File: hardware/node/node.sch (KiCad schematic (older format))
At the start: 48 parts, among them J1 IN, J10 ICSP, J30 PUMP, J60 OVF, Q0 SI2323DS, U1 ATmega328P-AU, U2 LMC555xM, U3 TPS22810, U4 P82B96

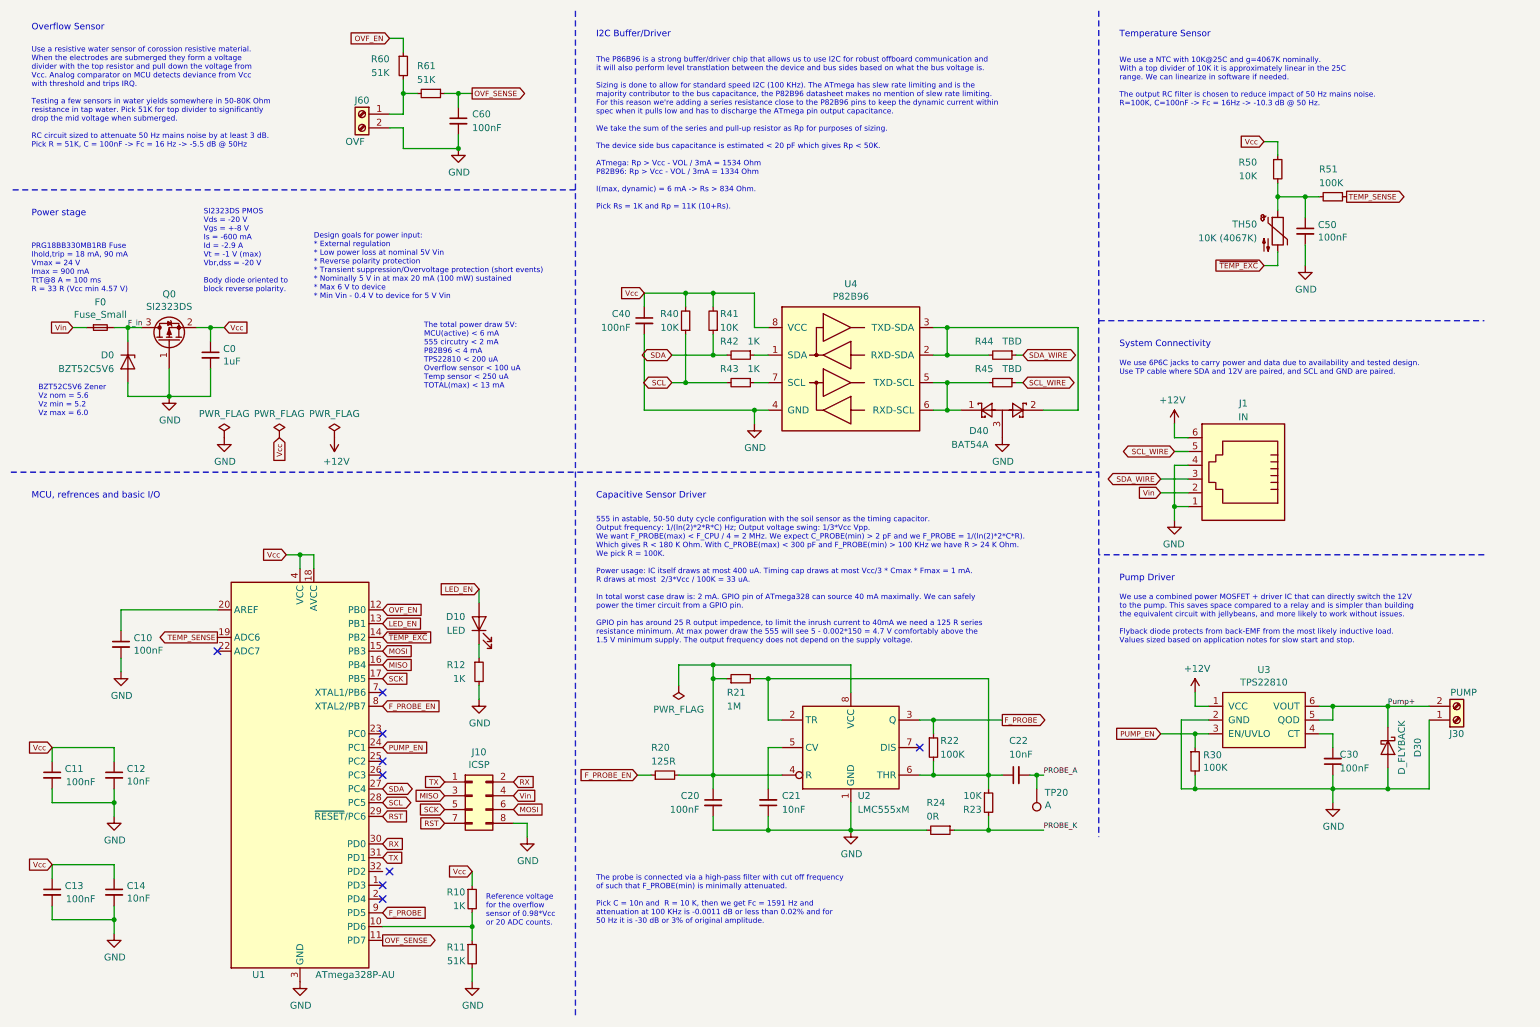
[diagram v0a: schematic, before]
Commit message: Updating layout of node and art.
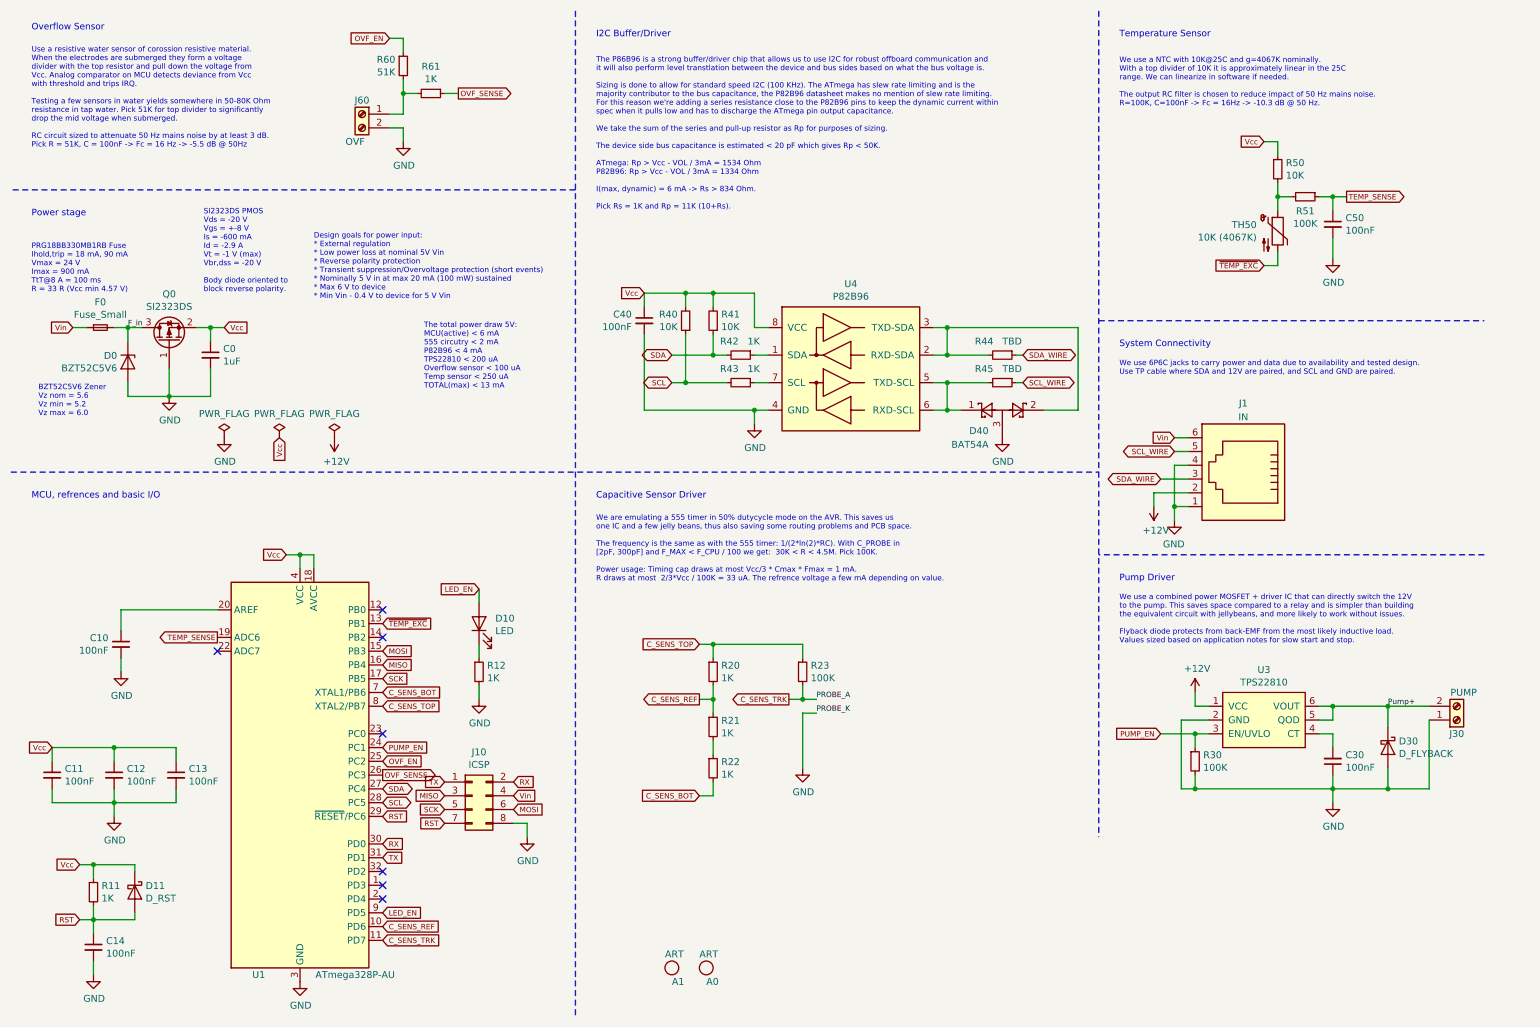
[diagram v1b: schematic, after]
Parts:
- removed C20, C60: 100nF, Capacitor_SMD:C_0603_1608Metric_Pad1.05x0.95mm_HandSolder, symbol Device:C_Small
- removed C21, C22: 10nF, Capacitor_SMD:C_0603_1608Metric_Pad1.05x0.95mm_HandSolder, symbol Device:C_Small
- removed R10: 1K, Resistor_SMD:R_0603_1608Metric_Pad1.05x0.95mm_HandSolder, symbol Device:R_Small
- removed R20: 125R, Resistor_SMD:R_0603_1608Metric_Pad1.05x0.95mm_HandSolder, symbol Device:R_Small
- removed R24: 0R, Resistor_SMD:R_0603_1608Metric_Pad1.05x0.95mm_HandSolder, symbol Device:R_Small
- removed TP20: A, TestPoint:TestPoint_Pad_D1.0mm, symbol Connector:TestPoint
- removed U2: LMC555xM, Package_SO:SOIC-8_3.9x4.9mm_P1.27mm, symbol Timer:LMC555xM
- added A0: ART, emilibeda:waterino_small_12_3mm, symbol emilibeda:ART
- added A1: ART, emilibeda:OSH_7_3mm, symbol emilibeda:ART
- added D11: D_RST, Diode_SMD:D_SOD-123, symbol Device:D_Schottky
- added R21: 1K, Resistor_SMD:R_0603_1608Metric_Pad1.05x0.95mm_HandSolder, symbol Device:R_Small
- C12, C14: value 10nF -> 100nF
- R11, R61: value 51K -> 1K
- R20: renamed from R21; value 1M -> 1K
- R22: value 100K -> 1K
- R23: value 10K -> 100K
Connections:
- net F_PROBE_EN is gone; now on net C_SENS_TOP: U1.8 (XTAL2/PB7)
- net +12V: now also J1.2; no longer J1.6
- net GND: no longer R11.2
- net LED_EN: now also U1.9 (PD5); no longer U1.13 (PB1)
- net OVF_EN: now also U1.25 (PC2); no longer U1.12 (PB0)
- net OVF_SENSE: now also U1.26 (PC3); no longer U1.11 (PD7)
- net RST: now also C14.1, R11.2, D11.2 (A)
- net TEMP_SENSE: now also C50.1
- net Vcc: now also R11.1, D11.1 (K); no longer C14.1
- net Vin: now also J1.6; no longer J1.2
- net ~TEMP_EXC: now also U1.13 (PB1); no longer U1.14 (PB2)
- net C_SENS_REF: now reaches U1.10 (PD6)
- net C_SENS_REF: now also R20.2, R21.1; no longer R11.1
- net C_SENS_BOT: now reaches U1.7 (XTAL1/PB6)
- net C_SENS_BOT: now also R22.2
- net C_SENS_TOP: now reaches R20.1
- net C_SENS_TOP: now also R23.1
- net at R50.2, R51.2, TH50.1: no longer C50.1
- net F_PROBE: no longer names the net of R22.1
- net F_PROBE: now also R21.2; no longer U1.9 (PD5)
- net PROBE_K renamed C_SENS_TRK
- net C_SENS_TRK: now also U1.11 (PD7)
- no-connect marks 9 -> 7
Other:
- note added: "We are emulating a 555 timer in 50% dutycycle mode on the AVR. This saves us \none IC and a few jelly beans, thus also saving some routing problems and PCB space.\n\nThe frequency is the same as with the 555 timer: 1/(2*ln(2)*RC). With C_PROBE in \n[2pF, 300pF] and F_MAX < F_CPU / 100 we get: 30K < R < 4.5M. Pick 100K. \n\nPower usage: Timing cap draws at most Vcc/3 * Cmax * Fmax = 1 mA.\nR draws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"
- note removed: "555 in astable, 50-50 duty cycle configuration with the soil sensor as the timing capacitor.\nOutput frequency: 1/(ln(2)*2*R*C) Hz; Output voltage swing: 1/3*Vcc Vpp.\nWe want F_PROBE(max) < F_CPU / 4 = 2 MHz. We expect C_PROBE(min) > 2 pF and we F_PROBE = 1/(ln(2)*2*C*R).\nWhich gives R < 180 K Ohm. With C_PROBE(max) < 300 pF and F_PROBE(min) > 100 KHz we have R > 24 K Ohm.\nWe pick R = 100K.\n\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"
- note removed: "Reference voltage\nfor the overflow\nsensor of 0.98*Vcc\nor 20 ADC counts."
- note removed: "The probe is connected via a high-pass filter with cut off frequency \nof such that F_PROBE(min) is minimally attenuated. \n\nPick C = 10n and R = 10 K, then we get Fc = 1591 Hz and \nattenuation at 100 KHz is -0.0011 dB or less than 0.02% and for \n50 Hz it is -30 dB or 3% of original amplitude.\n\n"
- moved on the sheet: C13, C50, R20, R51
